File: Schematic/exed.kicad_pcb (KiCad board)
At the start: 2 copper layers, 117.2 x 115.1 mm, 136 parts, among them J1 BananaPlus, J10 PLLDivider, J11 CounterControl, J12 CounterOutput, J13 PLLOutput, J14 PLLOutput, J15 LogicLow, J2 BananaMinus, J3 ShiftInput, J4 XOR, J5 LogicHigh, J6 ShiftOutput, J7 Clocks, J8 Clocks, J9 PLLDivider, Q1 PN2222A, Q2 PN2222A, SW1 Manual, U1 LM7805_TO220, U2 NE555P, U3 74LS00, U4 74HC595, U5 NE555P, U6 4017, U7 4046

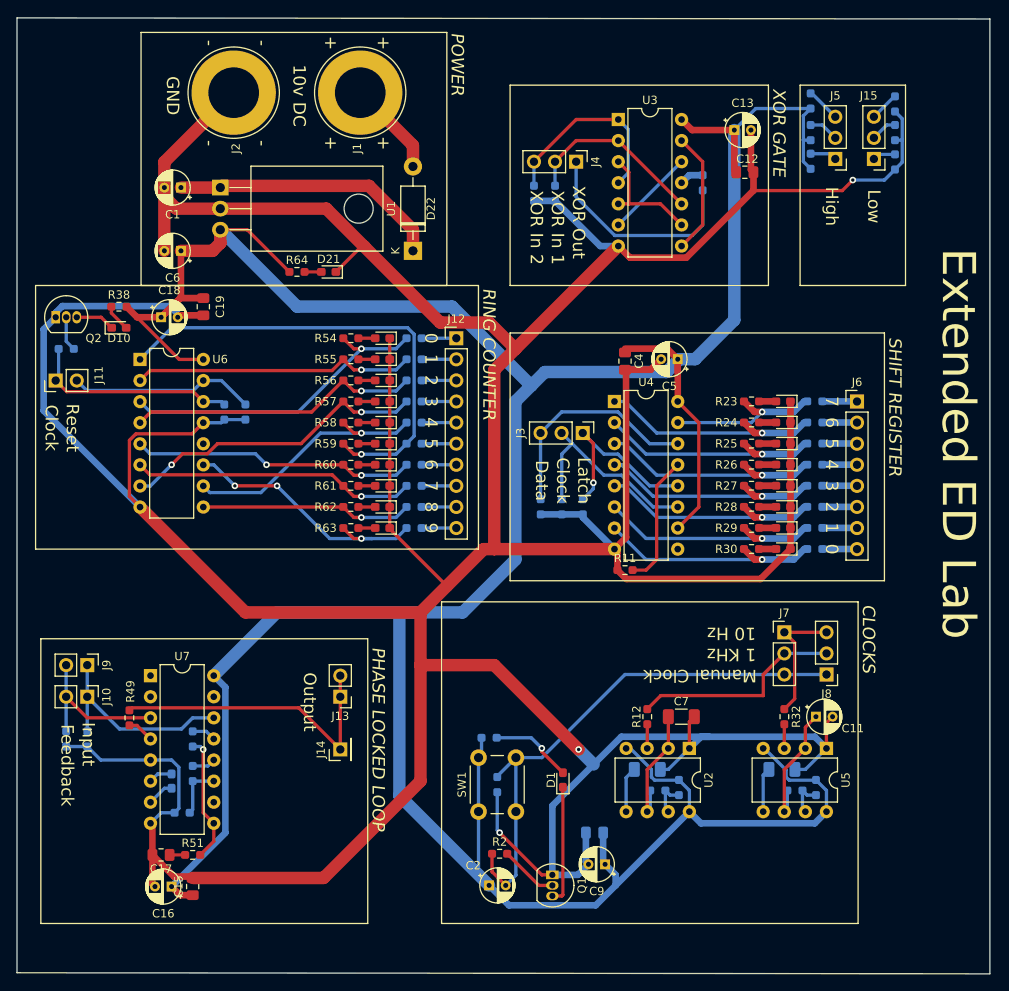
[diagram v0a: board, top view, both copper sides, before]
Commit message: Changed footprint of electrolytic to smd 0603
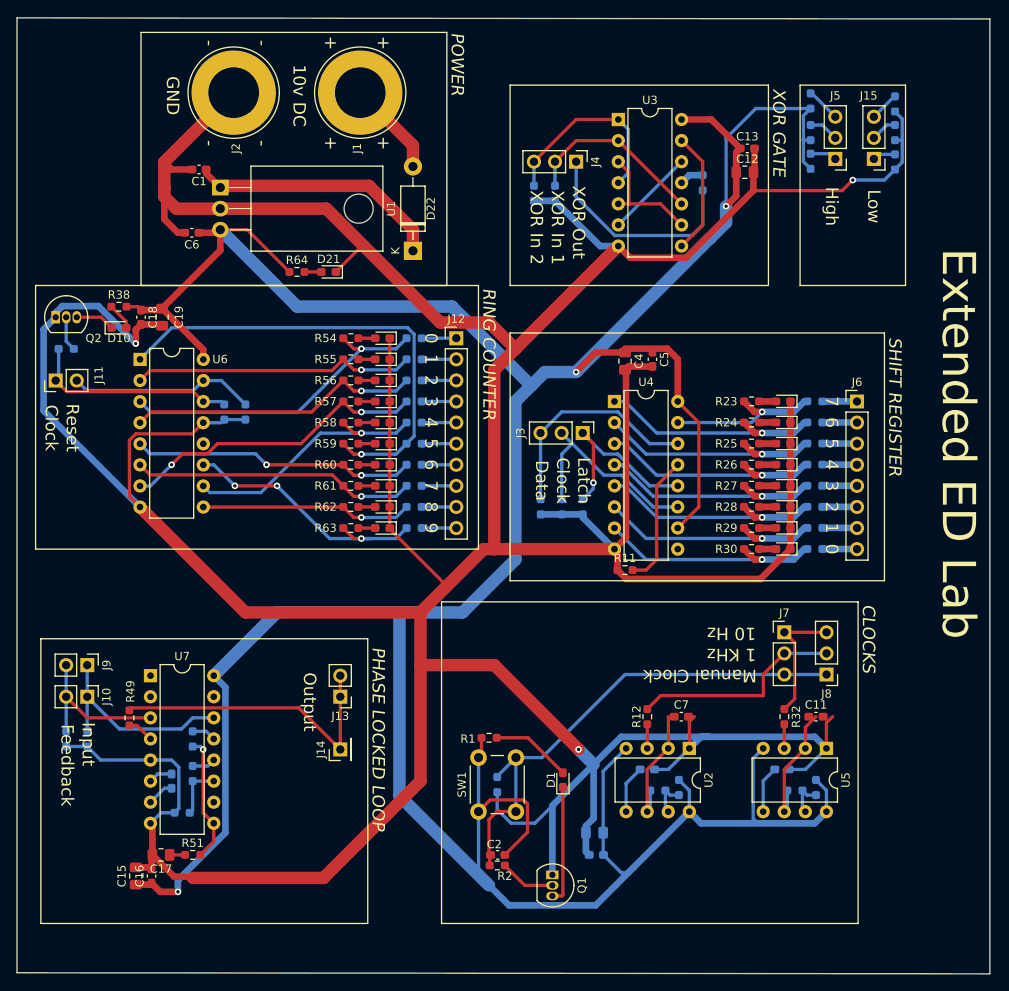
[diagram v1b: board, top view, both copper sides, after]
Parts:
- C1, C11, C13, C16, C18, C2, C5, C6: footprint Capacitor_THT:CP_Radial_D4.0mm_P2.00mm -> Capacitor_SMD:C_0603_1608Metric_Pad1.08x0.95mm_HandSolder
- C10, C3, C7: footprint Capacitor_SMD:C_1206_3216Metric_Pad1.33x1.80mm_HandSolder -> Capacitor_SMD:C_0603_1608Metric_Pad1.08x0.95mm_HandSolder
- C9: footprint Capacitor_THT:CP_Radial_D4.0mm_P2.00mm -> Capacitor_SMD:C_0603_1608Metric_Pad1.08x0.95mm_HandSolder; moved to B.Cu
- R1: moved to F.Cu
- moved C15 6.97 mm to (114.3, 133.3)
- moved C19 5.12 mm to (117.5, 66.0)
- moved C2 3.81 mm to (157.9, 130.8), turned to 180 degrees
- moved C1 3.08 mm to (121.9, 48.3)
- moved C5 3.05 mm to (176.5, 71.1), turned to -90 degrees
- moved C16 2.72 mm to (116.2, 133.3), turned to 90 degrees
- moved C13 2.71 mm to (188.0, 45.7)
- moved C6 2.54 mm to (121.1, 55.9)
- moved C18 2.42 mm to (114.9, 66.1), turned to -90 degrees
- moved C9 1.54 mm to (169.8, 130.8)
- moved R2 1.44 mm to (157.8, 132.1)
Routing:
- net +5V: track 436.6 -> 451.6 mm, vias 0 -> 3
- net Net-(C2-Pad2): track 65.2 -> 60.6 mm
- net GND: track 643.7 -> 640.5 mm
- net Net-(C1-Pad1): track 32.8 -> 30.9 mm
- net Net-(D1-Pad2): track 9.95 -> 9.72 mm, vias 1 -> 0
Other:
- board text added: "ExED v0.0 Licensed under GPL v3 github.com/lucaci32u4/ExED lucaci32u4.xyz/pages/ExED"
- board text removed: "Licensed under GPL v3 github.com/lucaci32u4/ExED lucaci32u4.xyz/pages/ExED"

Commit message: Added logo and bumped version
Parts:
- added G***: LOGO, LOGO, B.Cu at (212.1, 41.9)
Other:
- board text added: "ExED v0.1 Licensed under GPL v3 github.com/lucaci32u4/ExED lucaci32u4.xyz/pages/ExED"
- board text removed: "ExED v0.0 Licensed under GPL v3 github.com/lucaci32u4/ExED lucaci32u4.xyz/pages/ExED"

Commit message: Final version v0.1
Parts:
- removed R37: 10M, Resistor_SMD:R_0603_1608Metric_Pad0.98x0.95mm_HandSolder
- C10, C14, C3, C8, C9, R10, R13, R14, R15, R16, R17, R18, R19, R20, R21, R22, R31, R33, R34, R35, R36, R39, R4, R40, R41, R42, R43, R44, R45, R46, R47, R48, R5, R50, R52, R53, R6, R65, R66, R67, R68, R69, R7, R70, R8, R9: moved to F.Cu
- R3: value 500 -> 330; moved to F.Cu
- moved R31 12.9 mm to (170.2, 53.5), turned to 90 degrees
- moved R1 8.84 mm to (164.1, 121.8), turned to 90 degrees
- moved C10 8.79 mm to (199.8, 124.8), turned to -90 degrees
- moved C3 8.54 mm to (183.3, 124.8), turned to -90 degrees
- moved R40 7.39 mm to (110.7, 111.3), turned to -90 degrees
- moved R39 6.76 mm to (112.3, 111.3), turned to -90 degrees
- moved R46 6.75 mm to (126.2, 121.3)
- moved R5 6.55 mm to (160.4, 56.0), turned to 90 degrees
- moved R36 6.14 mm to (113.8, 126.5), turned to -90 degrees
- moved J9 5.75 mm to (105.2, 112.7), turned to 180 degrees
- moved R3 5.38 mm to (158.0, 117.0), turned to 0 degrees
- moved R21 5.11 mm to (196.8, 127.8), turned to 180 degrees
- moved C14 4.99 mm to (113.8, 123.2)
- moved R8 4.94 mm to (179.7, 127.6), turned to 180 degrees
- moved R22 4.71 mm to (193.5, 127.8)
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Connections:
- J10 pad 1: Net-(J10-Pad1) -> Net-(J10-Pin_1)
- J10 pad 2: Net-(J10-Pad2) -> Net-(J10-Pin_1)
- J9 pad 1: Net-(J10-Pad1) -> Net-(J9-Pin_1)
- J9 pad 2: Net-(J10-Pad2) -> Net-(J9-Pin_1)
- R39 pad 2: Net-(J10-Pad1) -> Net-(J10-Pin_1)
- R40 pad 2: Net-(J10-Pad2) -> Net-(J9-Pin_1)
- U7 pad 12: Net-(R37-Pad2) -> unconnected-(U7-R2-Pad12)
- U7 pad 14: Net-(J10-Pad1) -> Net-(J10-Pin_1)
- U7 pad 3: Net-(J10-Pad2) -> Net-(J9-Pin_1)
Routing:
- net Net-(J10-Pad1): track 25.8 -> 0.00 mm
- net Net-(J10-Pin_1): track 0.00 -> 23.9 mm
- net Net-(J9-Pin_1): track 0.00 -> 20.7 mm, vias 0 -> 1
- net Net-(J10-Pad2): track 19.2 -> 0.00 mm
- net Net-(J4-Pin_1): track 26.1 -> 8.54 mm
- net GND: track 640.5 -> 657.3 mm, vias 3 -> 5
- net unconnected-(U7-R2-Pad12): track 0.00 -> 14.3 mm, vias 0 -> 1
- net Net-(R31-Pad1): track 2.92 -> 13.9 mm, vias 0 -> 1
- net Net-(J4-Pin_2): track 22.3 -> 30.8 mm
- net Net-(D1-A): track 9.72 -> 1.67 mm
- net Net-(U5-CV): track 5.67 -> 13.7 mm
- net Net-(U2-CV): track 5.79 -> 13.4 mm
- net Net-(U7-R1): track 6.50 -> 11.5 mm, vias 0 -> 1
- net Net-(U7-VCOin): track 15.3 -> 10.3 mm, vias 1 -> 0
- net Net-(J3-Pin_2): track 24.9 -> 29.2 mm
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- added copper zone on B.Cu, net +5V
- added copper zone on F.Cu, net GND
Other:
- board text added: "ExED v0.1 Licensed under GPL v3 github.com/lucaci32u4/ExED lucaciresearch.net/pages/ExED"
- board text removed: "ExED v0.1 Licensed under GPL v3 github.com/lucaci32u4/ExED lucaci32u4.xyz/pages/ExED"
